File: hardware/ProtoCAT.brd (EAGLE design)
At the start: 59.7 x 53.3 mm, 54 parts, among them U1 ARDUINO, U3 TB6612FNG

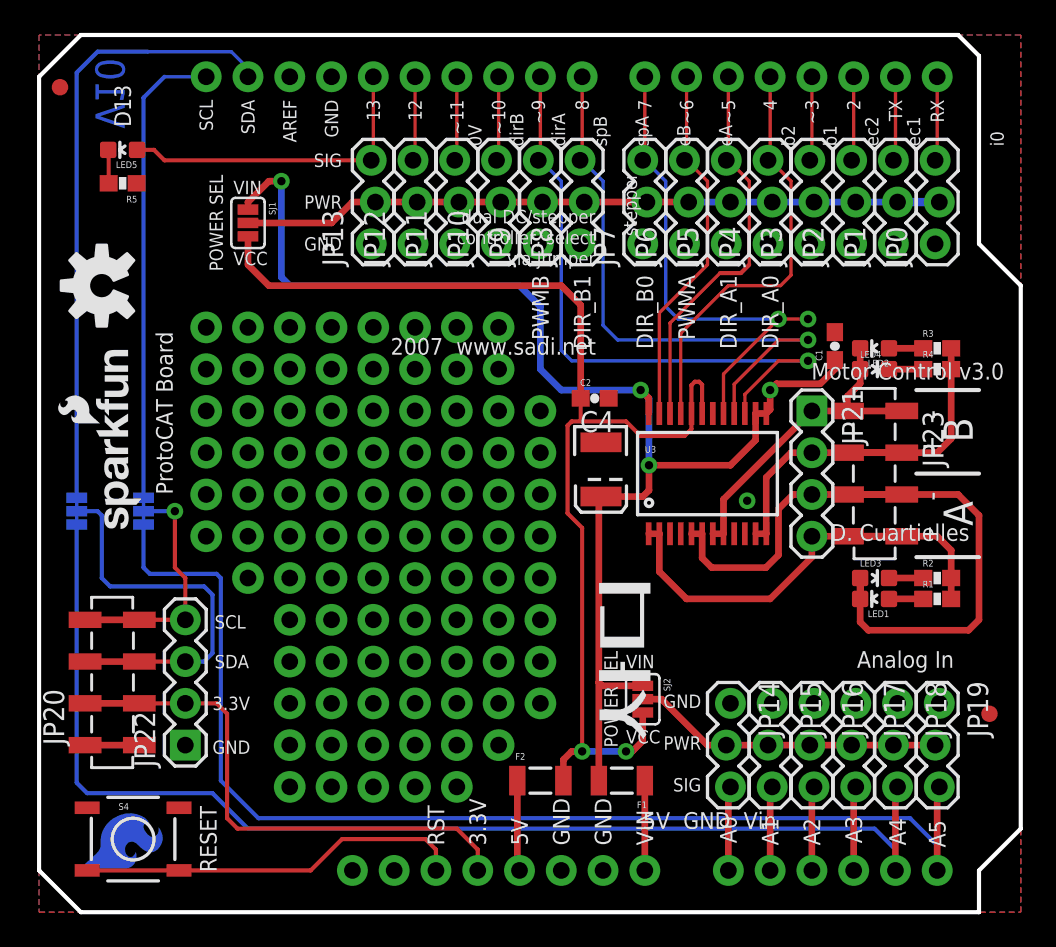
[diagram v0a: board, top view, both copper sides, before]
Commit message: Updated Silk and moved Motor connections
Updated the silk name to Ludus ProtoShield and moved the motor
connections below the SMD headers
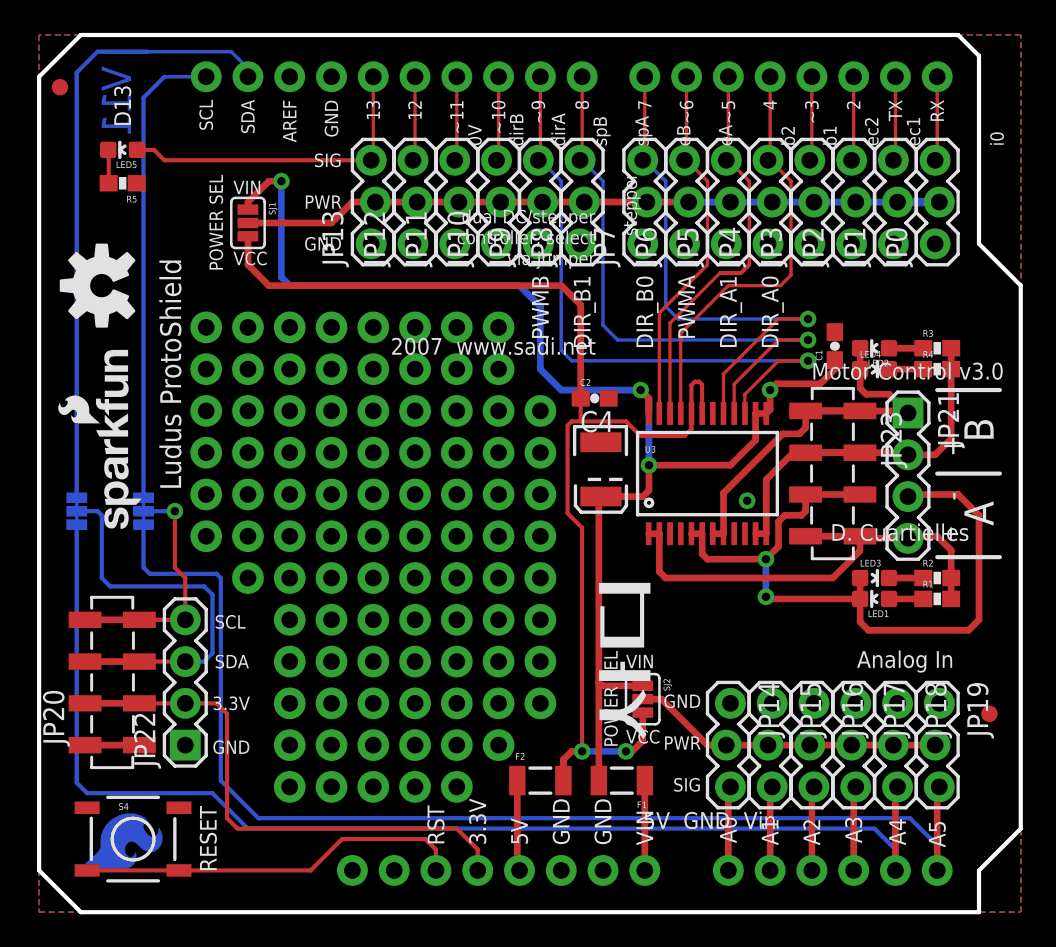
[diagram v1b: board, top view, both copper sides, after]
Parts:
- moved LOGO4 52.6 mm to (6.86, 43.7), turned to 270 degrees
- moved JP21 5.84 mm to (52.8, 30.4)
- moved U$1 5.24 mm to (39.4, 20.3), turned to 90 degrees
- moved JP23 2.54 mm to (48.3, 30.5)
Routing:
- net BOUT2: track 16.6 -> 23.0 mm
- net BIN1: track 30.8 -> 32.6 mm, vias 2 -> 1
- net AOUT1: track 27.3 -> 26.2 mm
- net AOUT2: track 41.2 -> 41.1 mm, vias 0 -> 2
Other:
- board text added: "Ludus ProtoShield"
- board text added: "V11"
- board text removed: "ProtoCAT Board"
- board text removed: "V10"
